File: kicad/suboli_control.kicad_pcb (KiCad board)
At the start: 2 copper layers, 0 parts

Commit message: R6: initial PCB placement (41 parts, outline, mounting holes)
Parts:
- added A2: OPA1622 dual op-amp on DIP-8 adapter, Package_DIP:DIP-8_W7.62mm_Socket, F.Cu at (100.0, 48.0)
- added C1: 1000 uF / 35 V bulk, Capacitor_THT:CP_Radial_D16.0mm_P7.50mm, F.Cu at (18.0, 42.0)
- added C10: 1 uF film R input coupling, Capacitor_THT:C_Rect_L7.2mm_W4.5mm_P5.00mm, F.Cu at (78.0, 66.0)
- added C11: 470uF/25V L output coupling, Capacitor_THT:CP_Radial_D10.0mm_P5.00mm, F.Cu at (66.0, 70.0)
- added C12: 470uF/25V R output coupling, Capacitor_THT:CP_Radial_D10.0mm_P5.00mm, F.Cu at (70.0, 46.0)
- added C2: 100 nF main bypass, Capacitor_THT:C_Disc_D7.5mm_W4.4mm_P5.00mm, F.Cu at (33.0, 38.0)
- added C3: 1000 uF / 25 V HP branch bulk, Capacitor_THT:CP_Radial_D10.0mm_P5.00mm, F.Cu at (86.0, 38.0)
- added C4: 100 nF HP branch bypass, Capacitor_THT:C_Disc_D7.5mm_W4.4mm_P5.00mm, F.Cu at (82.0, 49.0)
- added C5: 10 uF A2 V+ bulk decouple, Capacitor_THT:CP_Radial_D5.0mm_P2.00mm, F.Cu at (112.0, 40.0)
- added C6: 10 uF VGND decouple, Capacitor_THT:CP_Radial_D5.0mm_P2.00mm, F.Cu at (98.0, 28.0)
- added C7: 100 nF A2 V+ bypass, Capacitor_THT:C_Disc_D7.5mm_W4.4mm_P5.00mm, F.Cu at (100.0, 60.0)
- added C8: 100 nF VGND bypass, Capacitor_THT:C_Disc_D7.5mm_W4.4mm_P5.00mm, F.Cu at (86.0, 58.0)
- added C9: 1 uF film L input coupling, Capacitor_THT:C_Rect_L7.2mm_W4.5mm_P5.00mm, F.Cu at (74.0, 58.0)
- added D1: SB560 Schottky reverse-polarity diode, Diode_THT:D_DO-201AD_P15.24mm_Horizontal, F.Cu at (37.0, 24.0)
- added F1: PPTC fuse ~3 A, suboli_control:PPTC_LP30-300_P7.60mm, F.Cu at (16.0, 24.0)
- added FB1: Ferrite bead >=1 A, Inductor_THT:L_Axial_L12.0mm_D5.0mm_P15.24mm_Horizontal_Fastron_MISC, F.Cu at (16.0, 56.0)
- added J1: DC barrel jack panel header 5.5x2.5, Connector_Phoenix_MSTB:PhoenixContact_MSTBA_2,5_2-G-5,08_1x02_P5.08mm_Horizontal, F.Cu at (15.0, 10.0)
- added J2: 3.5 mm TRS input panel header, Connector_JST:JST_XH_B3B-XH-A_1x03_P2.50mm_Vertical, F.Cu at (15.0, 87.0)
- added J4: 3.5 mm TRS headphone panel header, Connector_JST:JST_XH_B3B-XH-A_1x03_P2.50mm_Vertical, F.Cu at (119.0, 52.0)
- added J5: MA12070 module power, Connector_Phoenix_MSTB:PhoenixContact_MSTBA_2,5_2-G-5,08_1x02_P5.08mm_Horizontal, F.Cu at (72.0, 11.0)
- added J6: MA12070 module audio in, Connector_JST:JST_XH_B3B-XH-A_1x03_P2.50mm_Vertical, F.Cu at (96.0, 11.0)
- added LED1: Power LED, LED_THT:LED_D5.0mm, F.Cu at (54.0, 36.0)
- added LED2: LL-504WC2EW61ED warm white 5mm, LED_THT:LED_D5.0mm, F.Cu at (36.0, 66.0)
- added LED3: LL-504WC2EW61ED warm white 5mm, LED_THT:LED_D5.0mm, F.Cu at (50.0, 66.0)
- added MH1: MountingHole_3.2mm_M3, MountingHole:MountingHole_3.2mm_M3, F.Cu at (7.00, 7.00)
- added MH2: MountingHole_3.2mm_M3, MountingHole:MountingHole_3.2mm_M3, F.Cu at (118.0, 7.00)
- added MH3: MountingHole_3.2mm_M3, MountingHole:MountingHole_3.2mm_M3, F.Cu at (7.00, 88.0)
- added MH4: MountingHole_3.2mm_M3, MountingHole:MountingHole_3.2mm_M3, F.Cu at (118.0, 88.0)
- added NT1: Only GND_SIG to GND_STAR connection, NetTie:NetTie-2_SMD_Pad0.5mm, F.Cu at (33.0, 44.0)
- added R1: 8.2 k LED resistor, Resistor_THT:R_Axial_DIN0207_L6.3mm_D2.5mm_P10.16mm_Horizontal, F.Cu at (54.0, 43.0)
- added R10: 1.2k, Resistor_THT:R_Axial_DIN0207_L6.3mm_D2.5mm_P10.16mm_Horizontal, F.Cu at (38.0, 58.0)
- added R2: 100k L input bias to VGND, Resistor_THT:R_Axial_DIN0207_L6.3mm_D2.5mm_P10.16mm_Horizontal, F.Cu at (92.0, 68.0)
- added R3: 100k R input bias to VGND, Resistor_THT:R_Axial_DIN0207_L6.3mm_D2.5mm_P10.16mm_Horizontal, F.Cu at (108.0, 68.0)
- added R4: 10 k L feedback, Resistor_THT:R_Axial_DIN0207_L6.3mm_D2.5mm_P10.16mm_Horizontal, F.Cu at (86.0, 74.0)
- added R5: 10 k L gain to VGND, Resistor_THT:R_Axial_DIN0207_L6.3mm_D2.5mm_P10.16mm_Horizontal, F.Cu at (102.0, 74.0)
- added R6: 10 k R feedback, Resistor_THT:R_Axial_DIN0207_L6.3mm_D2.5mm_P10.16mm_Horizontal, F.Cu at (72.0, 80.0)
- added R7: 10 k R gain to VGND, Resistor_THT:R_Axial_DIN0207_L6.3mm_D2.5mm_P10.16mm_Horizontal, F.Cu at (88.0, 80.0)
- added R8: 10 ohm L output series, Resistor_THT:R_Axial_DIN0207_L6.3mm_D2.5mm_P10.16mm_Horizontal, F.Cu at (104.0, 80.0)
- added R9: 10 ohm R output series, Resistor_THT:R_Axial_DIN0207_L6.3mm_D2.5mm_P10.16mm_Horizontal, F.Cu at (114.0, 62.0)
- added RV1: Dual-gang 10 k log tactile volume panel header, Connector_JST:JST_XH_B6B-XH-A_1x06_P2.50mm_Vertical, F.Cu at (40.0, 87.0)
- added RV2: Dual-gang 10 k log headphone volume panel header, Connector_JST:JST_XH_B6B-XH-A_1x06_P2.50mm_Vertical, F.Cu at (66.0, 87.0)
- added RV3: 3296W-10K, Potentiometer_THT:Potentiometer_Bourns_3296W_Vertical, F.Cu at (54.0, 58.0)
- added SW1: DPST power switch panel header, Connector_Phoenix_MSTB:PhoenixContact_MSTBA_2,5_4-G-5,08_1x04_P5.08mm_Horizontal, F.Cu at (42.0, 10.0)
- added TVS1: P6KE24A, Diode_THT:D_DO-15_P10.16mm_Horizontal, F.Cu at (56.0, 24.0)
- added U1: TLE2426ILP, Package_TO_SOT_THT:TO-92_Inline, F.Cu at (100.0, 37.0)
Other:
- board outline added: 125 x 95 mm
- board text removed: "SUBOLI schematic phase only - no board outline, footprints, placement, routing, zones, STEP, or Gerbers yet"

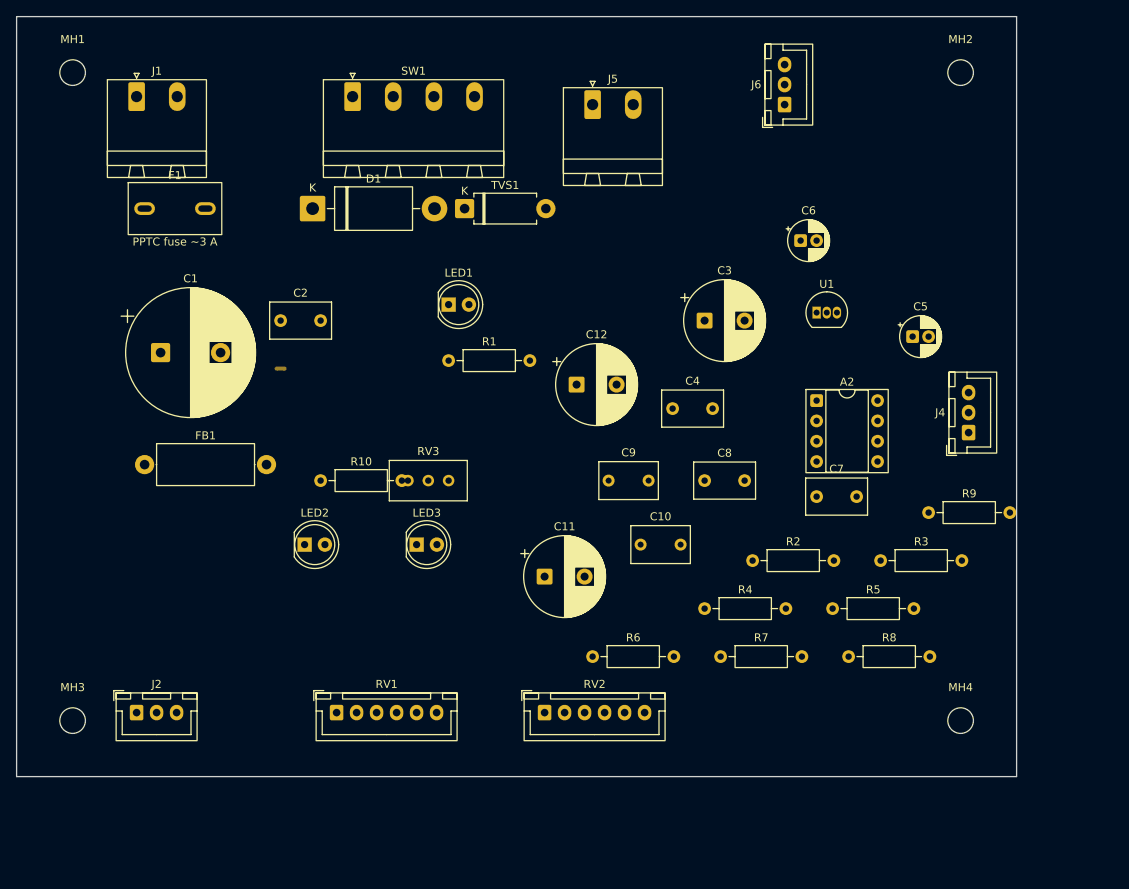
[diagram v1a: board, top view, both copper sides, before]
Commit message: R8: attempt auto-route of power + ground + glow nets
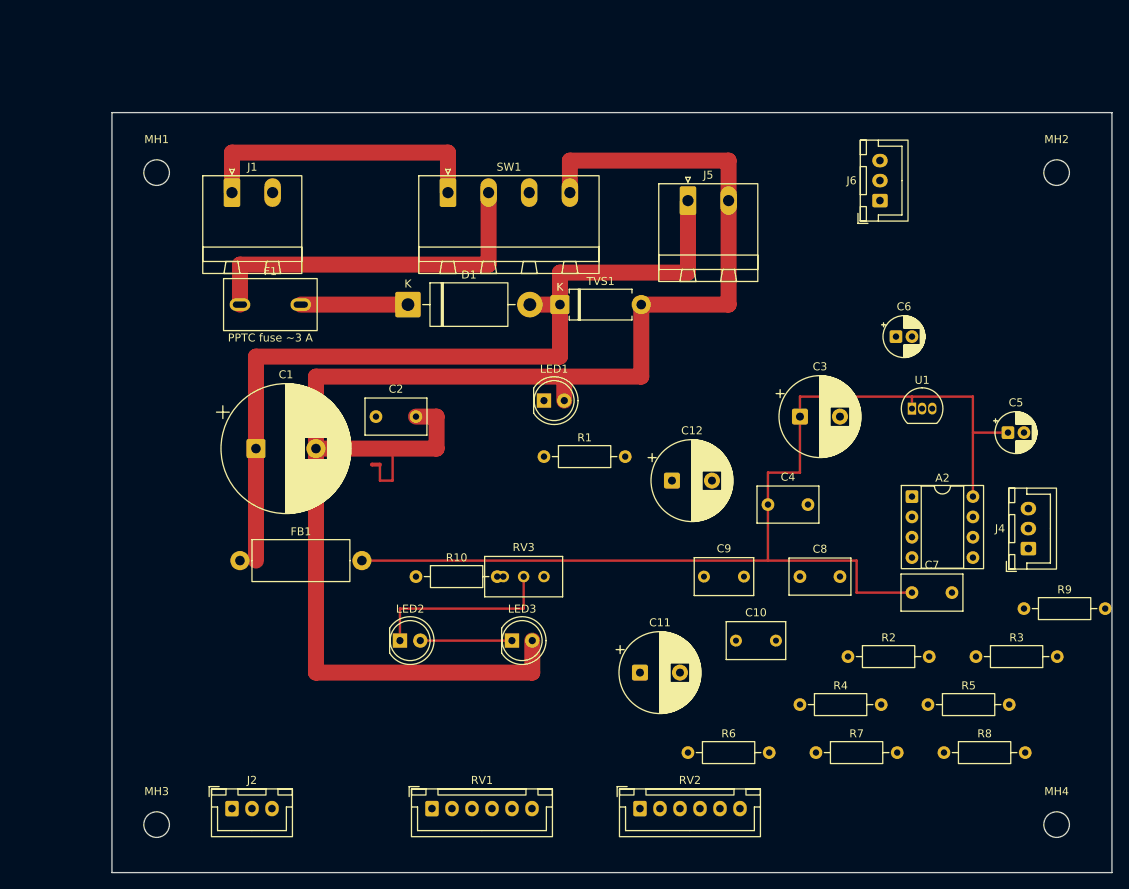
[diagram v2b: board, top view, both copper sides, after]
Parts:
- moved MH4 17.7 mm to (130.0, 101.0)
- moved MH2 17.3 mm to (130.0, 19.5)
- moved A2 16.9 mm to (111.9, 60.0)
- moved C1 16.9 mm to (29.9, 54.0)
- moved C10 16.9 mm to (89.9, 78.0)
- moved C11 16.9 mm to (77.9, 82.0)
- moved C12 16.9 mm to (81.9, 58.0)
- moved C2 16.9 mm to (44.9, 50.0)
- moved C3 16.9 mm to (97.9, 50.0)
- moved C4 16.9 mm to (93.9, 61.0)
- moved C5 16.9 mm to (123.9, 52.0)
- moved C6 16.9 mm to (109.9, 40.0)
- moved C7 16.9 mm to (111.9, 72.0)
- moved C8 16.9 mm to (97.9, 70.0)
- moved C9 16.9 mm to (85.9, 70.0)
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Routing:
- net /GND_STAR: track 0.00 -> 202.7 mm
- net /+19V_HP: track 0.00 -> 137.3 mm
- net /+19V: track 0.00 -> 102.8 mm
- net /+19V_SW: track 0.00 -> 45.1 mm
- net /+19V_RAW: track 0.00 -> 37.0 mm
- net /GLOW_B: track 0.00 -> 23.5 mm
- net /+19V_F: track 0.00 -> 13.4 mm
- net /GLOW_MID: track 0.00 -> 11.5 mm
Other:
- rule pad_to_mask_clearance: 0 -> 0.1

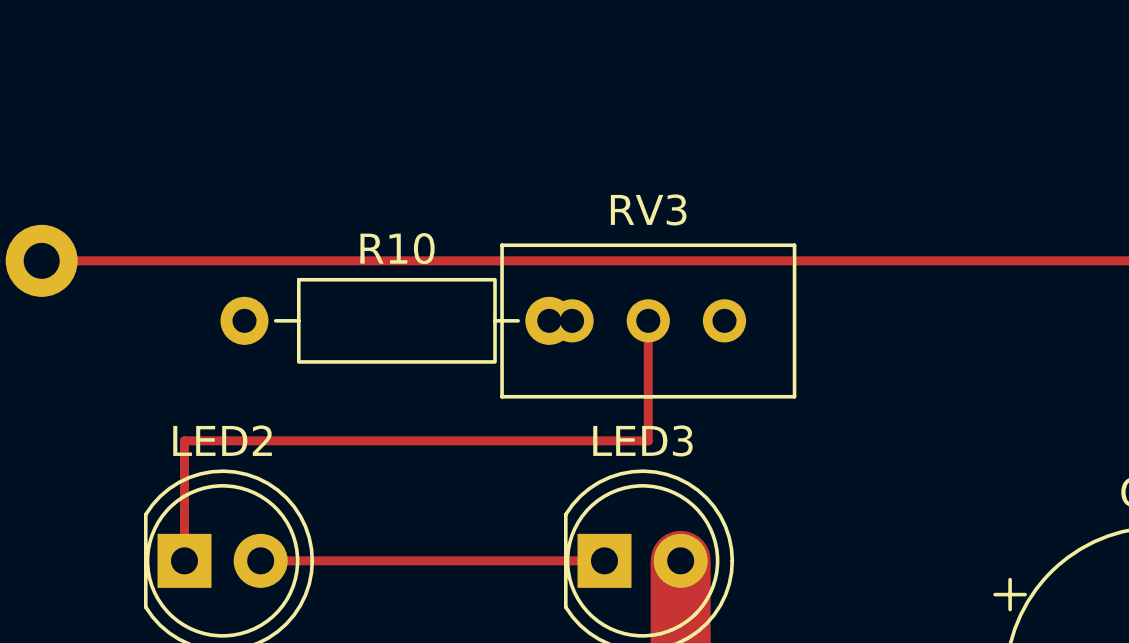
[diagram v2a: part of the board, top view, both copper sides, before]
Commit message: R8.1: fix glow trimmer short
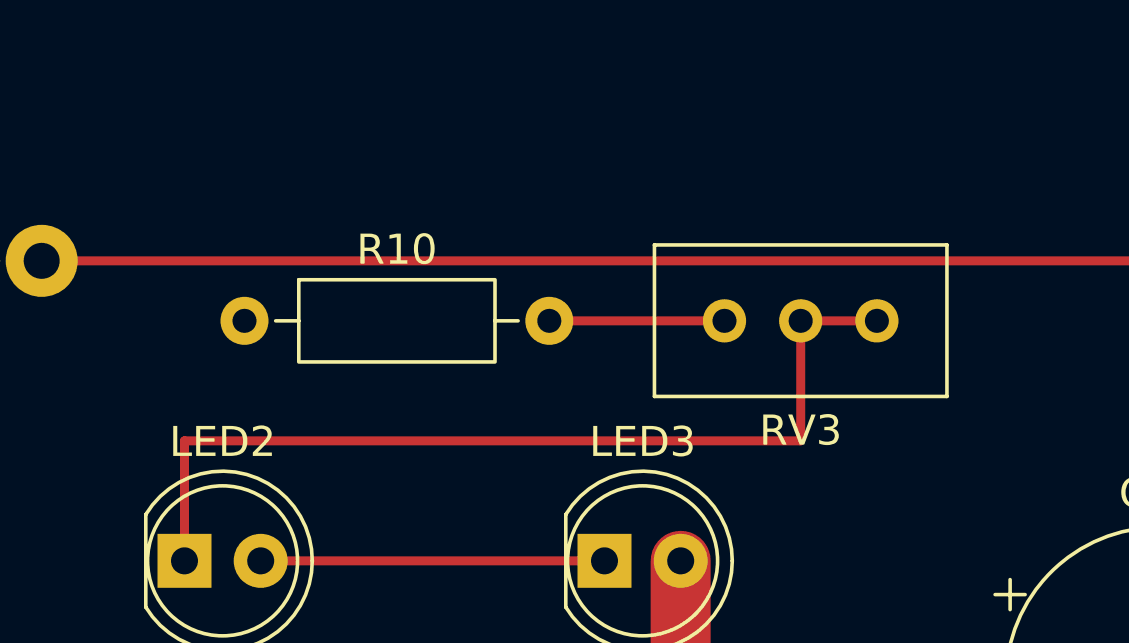
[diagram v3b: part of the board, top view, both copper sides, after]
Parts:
- turned RV3 to 180 degrees
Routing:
- net /GLOW_B: track 23.5 -> 31.1 mm
- net /GLOW_A: track 0.00 -> 5.84 mm
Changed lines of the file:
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@@
 	(footprint "Potentiometer_THT:Potentiometer_Bourns_3296W_Vertical"
 		(layer "F.Cu")
-		(at 65.92 70)
+		(at 65.92 70 180)
 		(descr "Potentiometer, vertical, Bourns 3296W, https://www.bourns.com/pdfs/3296.pdf")
 		(tags "Potentiometer vertical Bourns 3296W")
 		(property "Reference" "RV3"
-			(at -2.54 -3.66 0)
+			(at -2.54 -3.66 180)
 			(layer "F.SilkS")
 			(effects
@@
 		)
 		(property "Value" "3296W-10K"
-			(at -2.54 3.67 0)
+			(at -2.54 3.67 180)
 			(layer "F.Fab")
 			(effects
@@
 		)
 		(property "Datasheet" ""
-			(at 0 0 0)
+			(at 0 0 180)
 			(layer "F.Fab")
 			(hide yes)
@@
 		)
 		(property "Description" ""
-			(at 0 0 0)
+			(at 0 0 180)
 			(layer "F.Fab")
 			(hide yes)
@@
 		)
 		(property "Supplier" "HESTORE"
-			(at 0 0 0)
+			(at 0 0 180)
 			(layer "F.Fab")
 			(hide yes)
@@
 		)
 		(property "Supplier_PN" "100.412.47"
-			(at 0 0 0)
+			(at 0 0 180)
 			(layer "F.Fab")
 			(hide yes)
@@
 		)
 		(property "Manufacturer" ""
-			(at 0 0 0)
+			(at 0 0 180)
 			(layer "F.Fab")
 			(hide yes)
@@
 		)
 		(property "MPN" ""
-			(at 0 0 0)
+			(at 0 0 180)
 			(layer "F.Fab")
 			(hide yes)
@@
 		)
 		(property "Function" "Glow brightness set"
-			(at 0 0 0)
+			(at 0 0 180)
 			(layer "F.Fab")
 			(hide yes)
@@
 		)
 		(property "Wiring" "rheostat: pin 1 in, wiper pin 2 tied to pin 3 out"
-			(at 0 0 0)
+			(at 0 0 180)
 			(layer "F.Fab")
 			(hide yes)
@@
 		)
 		(property "KiLib_Generator" "potentiometer/THT"
-			(at 0 0 0)
+			(at 0 0 180)
 			(layer "F.SilkS")
 			(hide yes)
@@
 		)
 		(fp_text user "${REFERENCE}"
-			(at -3.175 0.005 0)
+			(at -3.175 0.005 180)
 			(layer "F.Fab")
 			(effects
@@
 		)
 		(pad "1" thru_hole circle
-			(at 0 0)
+			(at 0 0 180)
 			(size 1.44 1.44)
 			(drill 0.8)
@@
 		)
 		(pad "2" thru_hole circle
-			(at -2.54 0)
+			(at -2.54 0 180)
 			(size 1.44 1.44)
 			(drill 0.8)
@@
 		)
 		(pad "3" thru_hole circle
-			(at -5.08 0)
+			(at -5.08 0 180)
 			(size 1.44 1.44)
 			(drill 0.8)
@@
 	)
 	(segment
-		(start 63.38 70)
-		(end 63.38 74)
+		(start 68.46 70)
+		(end 68.46 74)
 		(width 0.3)
 		(layer "F.Cu")
@@
 	)
 	(segment
-		(start 63.38 74)
+		(start 68.46 74)
 		(end 47.92 74)
 		(width 0.3)
@@
 		(net "/GLOW_MID")
 	)
+	(segment
+		(start 60.08 70)
+		(end 65.92 70)
+		(width 0.3)
+		(layer "F.Cu")
+		(net "/GLOW_A")
+	)
+	(segment
+		(start 68.46 70)
+		(end 71 70)
+		(width 0.3)
+		(layer "F.Cu")
+		(net "/GLOW_B")
+	)
 	(embedded_fonts no)

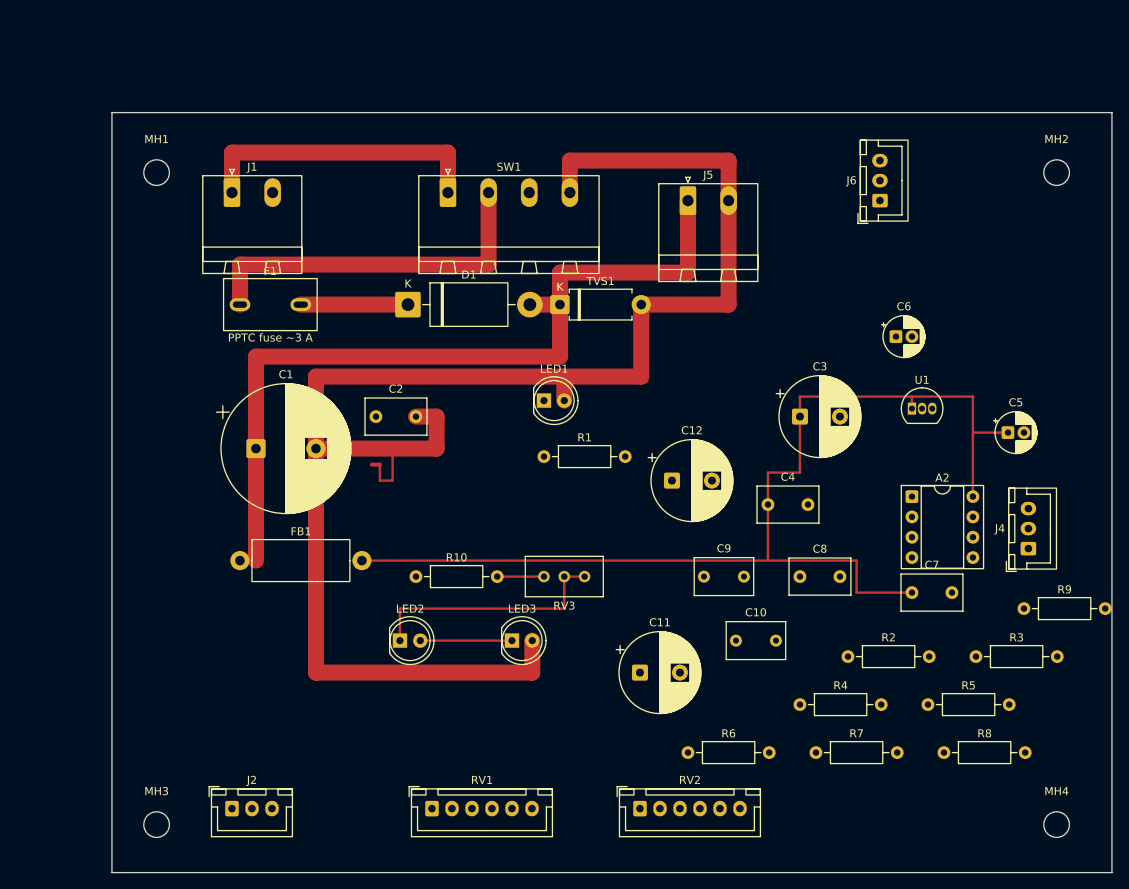
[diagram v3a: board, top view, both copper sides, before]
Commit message: R9: DRC clean - silkscreen + TO-92 mask fixes, 0 violations
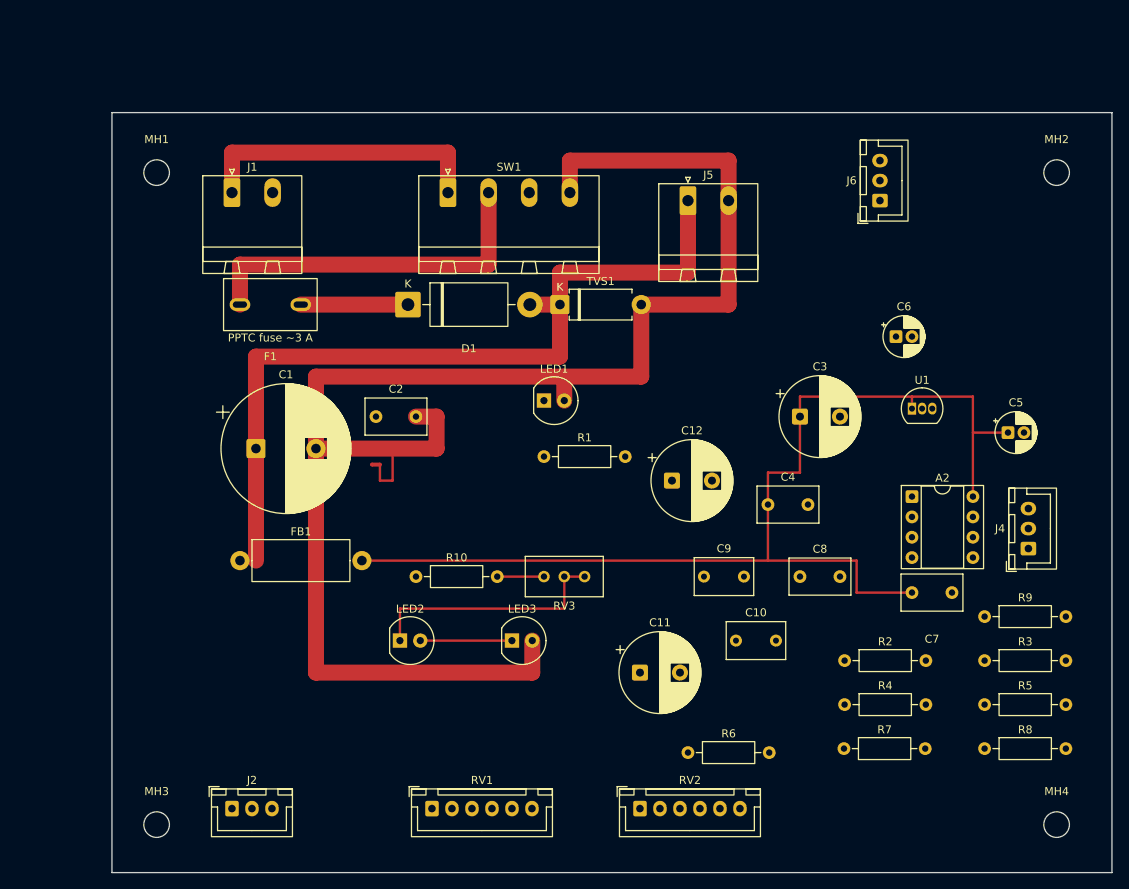
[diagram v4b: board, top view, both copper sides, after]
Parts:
- LED1, LED2, LED3: footprint LED_THT:LED_D5.0mm -> suboli_control:LED_D5.0mm_NoSilkCircle
- moved R5 7.08 mm to (121.0, 86.0)
- moved R4 5.58 mm to (103.5, 86.0)
- moved R8 5.10 mm to (121.0, 91.5)
- moved R9 5.02 mm to (121.0, 75.0)
- moved R7 3.54 mm to (103.4, 91.5)
- moved R3 1.19 mm to (121.0, 80.5)
- moved R2 0.65 mm to (103.5, 80.5)
